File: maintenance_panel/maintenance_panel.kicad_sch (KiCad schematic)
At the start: 14 parts, among them J1 Conn_02x13_Odd_Even, U3 74LS244, U4 74LS02

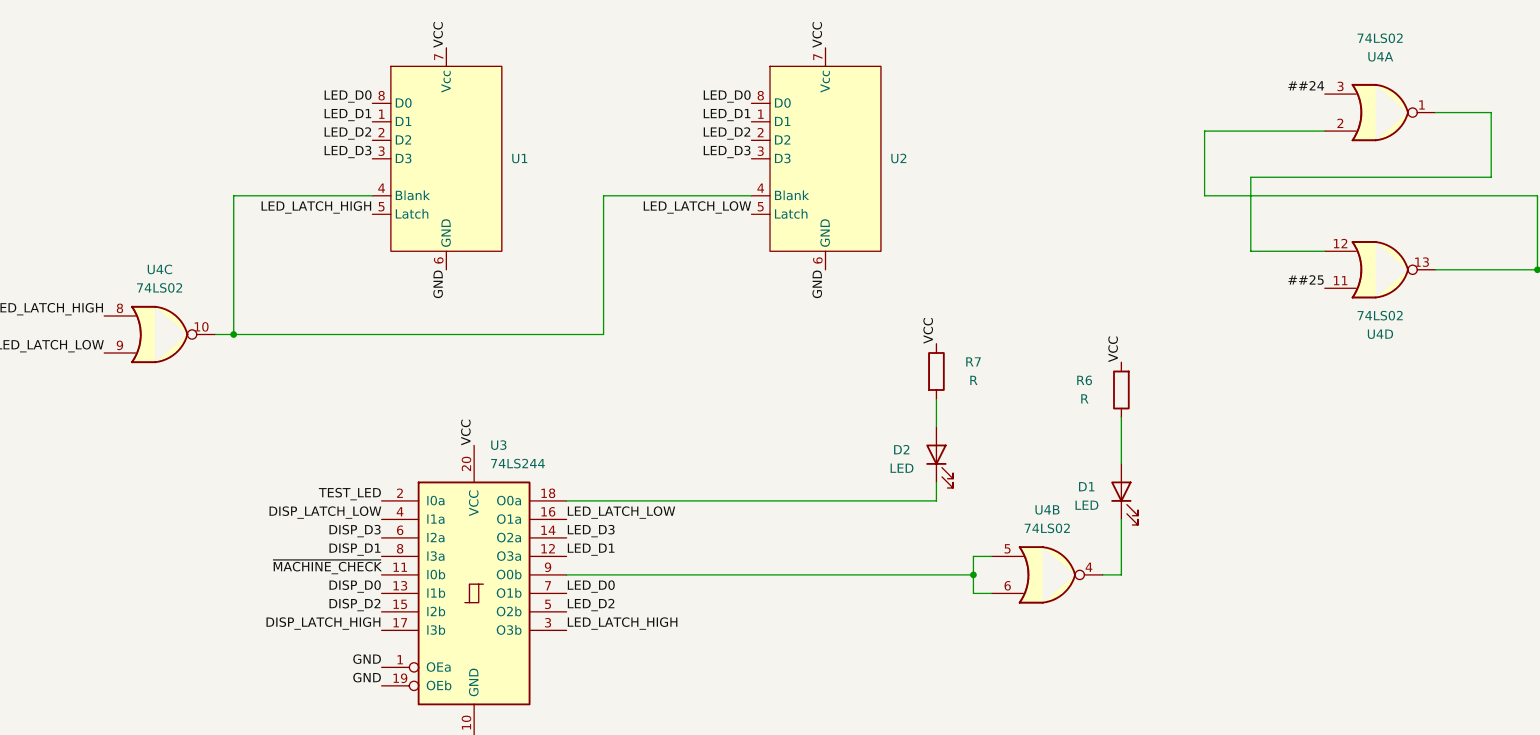
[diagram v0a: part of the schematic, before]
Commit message: Update KiCad version
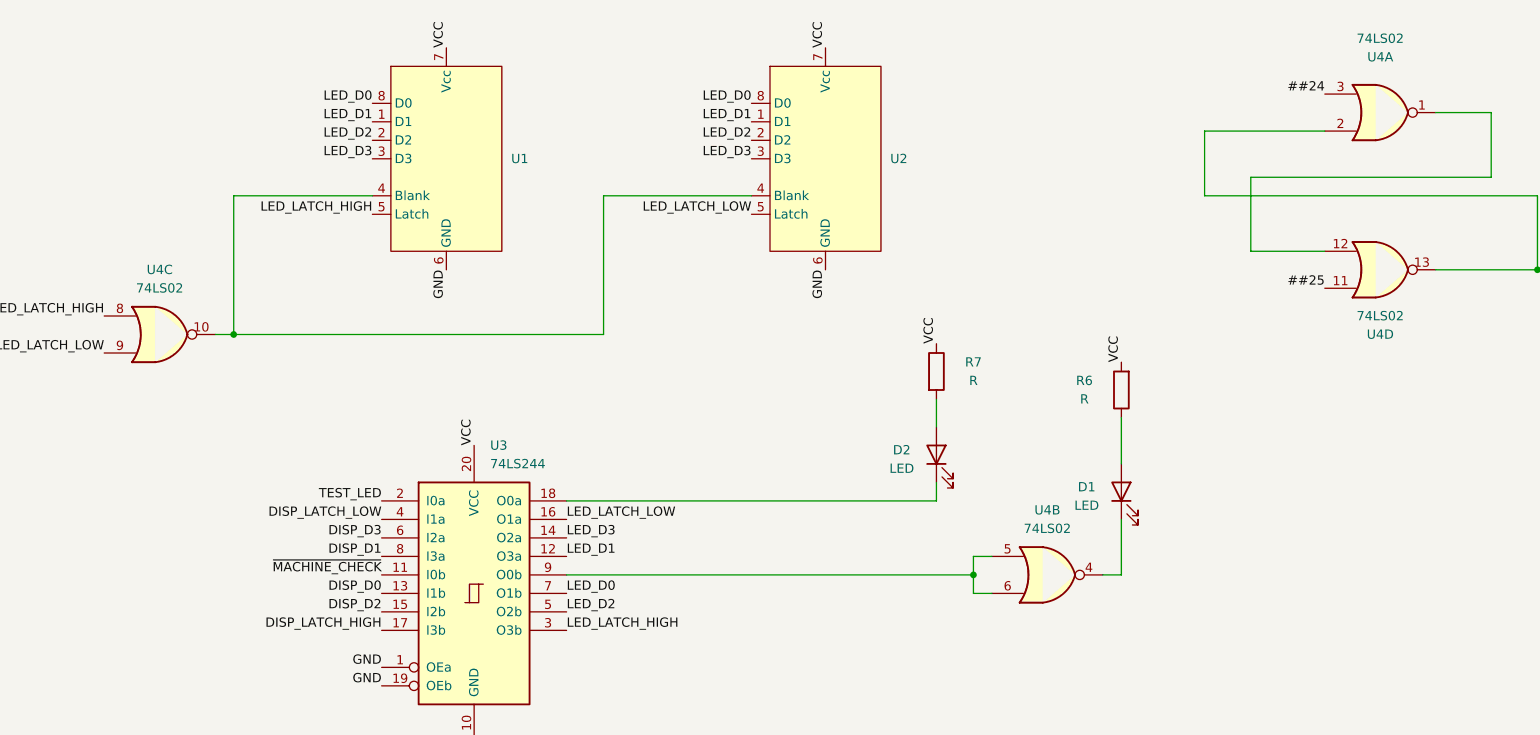
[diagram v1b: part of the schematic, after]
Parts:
- U1, U2: value ~ -> (none)
